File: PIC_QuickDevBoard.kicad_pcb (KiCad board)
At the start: 2 copper layers, 70.9 x 81.3 mm, 36 parts, among them J1 Conn_01x08_Pin, J10 VCC Lines, J2 Conn_01x08_Pin, J3 Conn_01x08_Pin, J4 PowerSource, J5 PICKitConnector, J6 USB_B_Micro, J7 PGEC_LINES, J8 PGED_LINES, J9 MCLR_LINES, SW1 SW_Push, U1 PIC24F, U2 PIC16F84, U3 LDA33A, U4 PIC16F1459-IP, Y1 Crystal

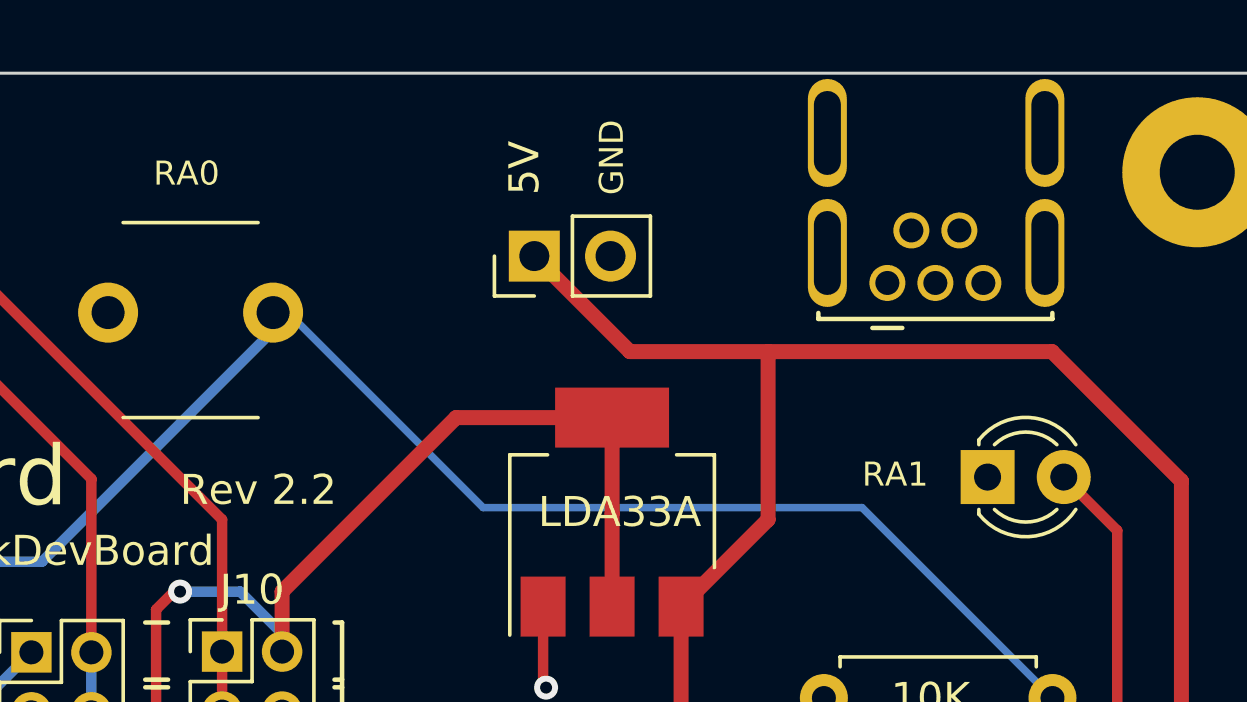
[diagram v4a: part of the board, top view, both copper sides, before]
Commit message: Rev2.3 - fixed mini-usb footprint and pcb routing power from it.
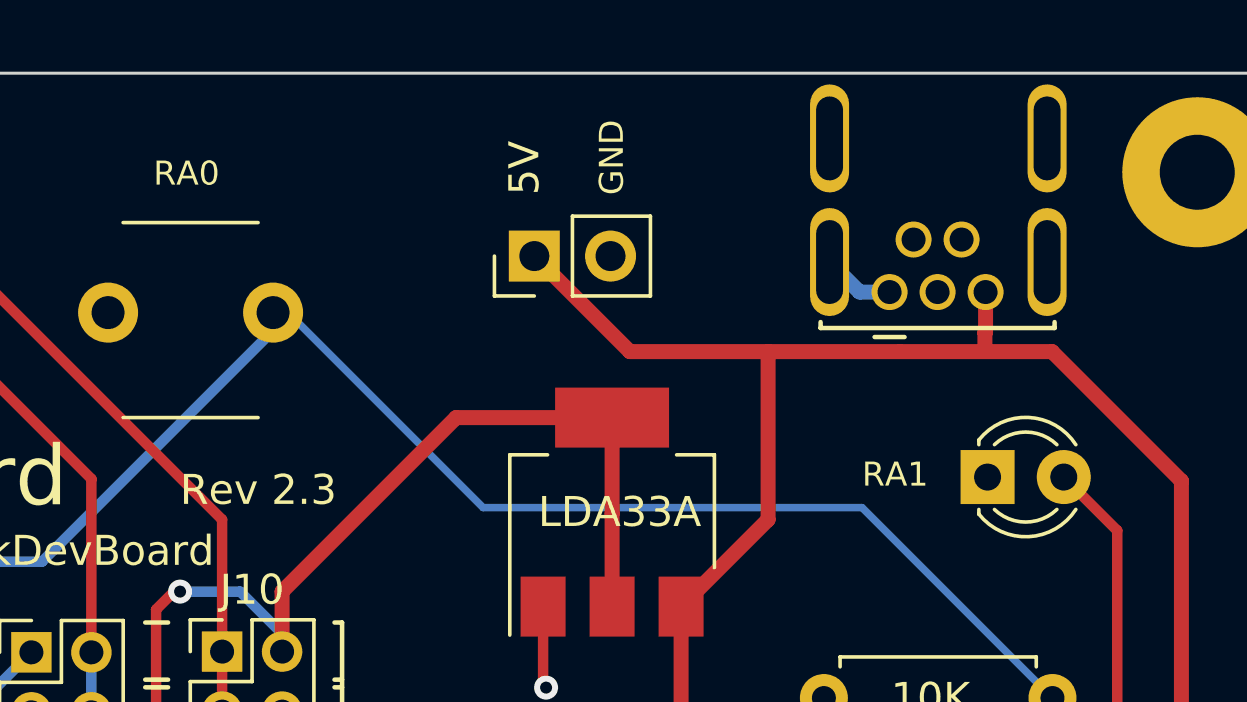
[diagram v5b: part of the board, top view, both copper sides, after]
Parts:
- moved J6 0.31 mm to (120.3, 40.3)
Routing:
- net GND: track 242.6 -> 245.1 mm
- net +5V: track 136.7 -> 138.7 mm
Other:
- board text added: "Rev 2.3"
- board text removed: "Rev 2.2"
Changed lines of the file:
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@@
 	(title_block
 		(title "PIC16/24 Programmer & Dev Board")
-		(date "2024-05-01")
-		(rev "2.2")
+		(date "2024-05-17")
+		(rev "2.3")
 		(company "RCC 2024")
 	)
@@
 	(net 39 "+5V")
 	(net 40 "+3.3V")
+	(net 41 "unconnected-(J6-ID-Pad4)")
+	(net 42 "unconnected-(J6-D--Pad2)")
+	(net 43 "unconnected-(J6-D+-Pad3)")
 	(footprint "Connector_PinHeader_2.00mm:PinHeader_2x03_P2.00mm_Vertical"
 		(layer "F.Cu")
@@
 	(footprint "Roni_Footprints:USB_Mini-B_Tensility_4Holes"
 		(layer "F.Cu")
-		(at 120.226 40.012)
+		(at 120.299813 40.314672)
 		(descr "http://www.tensility.com/pdffiles/54-00023.pdf")
 		(tags "usb mini receptacle vertical")
@@
 			)
 		)
+		(property ki_fp_filters "USB*")
+		(sheetname "Root")
+		(sheetfile "PIC_QuickDevBoard.kicad_sch")
 		(attr through_hole)
 		(fp_line
@@
 		)
 		(fp_line
-			(start -2.8 -6.82681)
+			(start -2.8 -7)
 			(end -2.8 1.5)
 			(stroke
@@
 		)
 		(fp_line
-			(start 6 -6.82681)
-			(end -2.8 -6.82681)
+			(start 6 -7)
+			(end -2.8 -7)
 			(stroke
 				(width 0.05)
@@
 		(fp_line
 			(start 6 1.5)
-			(end 6 -6.82681)
+			(end 6 -7)
 			(stroke
 				(width 0.05)
@@
 			)
 		)
-		(pad "" thru_hole circle
-			(at 0 0)
+		(pad "1" thru_hole circle
+			(at 3.2 0)
 			(size 1.2 1.2)
 			(drill 0.8)
 			(layers "*.Cu" "*.Mask")
 			(remove_unused_layers no)
+			(net 39 "+5V")
+			(pinfunction "VBUS")
+			(pintype "power_out")
 		)
-		(pad "" thru_hole circle
-			(at 0.8 -1.75)
+		(pad "2" thru_hole circle
+			(at 2.4 -1.75)
 			(size 1.2 1.2)
 			(drill 0.8)
 			(layers "*.Cu" "*.Mask")
 			(remove_unused_layers no)
+			(net 42 "unconnected-(J6-D--Pad2)")
+			(pinfunction "D-")
+			(pintype "bidirectional+no_connect")
 		)
-		(pad "" thru_hole circle
+		(pad "3" thru_hole circle
 			(at 1.6 0)
 			(size 1.2 1.2)
@@
 			(layers "*.Cu" "*.Mask")
 			(remove_unused_layers no)
+			(net 43 "unconnected-(J6-D+-Pad3)")
+			(pinfunction "D+")
+			(pintype "bidirectional+no_connect")
 		)
-		(pad "" thru_hole circle
-			(at 2.4 -1.75)
+		(pad "4" thru_hole circle
+			(at 0.8 -1.75)
 			(size 1.2 1.2)
 			(drill 0.8)
 			(layers "*.Cu" "*.Mask")
 			(remove_unused_layers no)
+			(net 41 "unconnected-(J6-ID-Pad4)")
+			(pinfunction "ID")
+			(pintype "passive+no_connect")
 		)
-		(pad "" thru_hole circle
-			(at 3.2 0)
+		(pad "5" thru_hole circle
+			(at 0 0)
 			(size 1.2 1.2)
 			(drill 0.8)
 			(layers "*.Cu" "*.Mask")
 			(remove_unused_layers no)
+			(net 1 "GND")
+			(pinfunction "GND")
+			(pintype "power_out")
 		)
 		(pad "6" thru_hole oval
-			(at -2 -5)
+			(at -2 -5.120687)
 			(size 1.3 3.6)
 			(drill oval 0.9 2.8)
@@
 		)
 		(pad "6" thru_hole oval
-			(at 5.25 -5)
+			(at 5.25 -5.120687)
 			(size 1.3 3.6)
 			(drill oval 0.9 2.8)
@@
 		)
 	)
-	(gr_text "Rev 2.2"
+	(gr_text "Rev 2.3"
 		(at 96.647 47.498 0)
 		(layer "F.SilkS")
@@
 	)
 	(segment
+		(start 120.222677 40.391808)
+		(end 120.299813 40.314672)
+		(width 0.5)
+		(layer "F.Cu")
+		(net 1)
+	)
+	(segment
 		(start 79.883 71.374)
 		(end 80.137 71.12)
@@
 	)
 	(segment
+		(start 119.299813 40.314672)
+		(end 118.299813 39.314672)
+		(width 0.5)
+		(layer "B.Cu")
+		(net 1)
+	)
+	(segment
 		(start 126.85 84.7)
 		(end 126.85 85.956)
@@
 	)
 	(segment
+		(start 120.299813 40.314672)
+		(end 119.299813 40.314672)
+		(width 0.5)
+		(layer "B.Cu")
+		(net 1)
+	)
+	(segment
 		(start 93.091 82.296)
 		(end 93.091 78.319)
@@
 	)
 	(segment
-		(start 125.714 42.3)
-		(end 116.25 42.3)
-		(width 0.5)
-		(layer "F.Cu")
-		(net 39)
-	)
-	(segment
 		(start 110.85 56.9)
 		(end 113.35 54.4)
@@
 	)
 	(segment
+		(start 123.499813 41.645167)
+		(end 123.499813 40.314672)
+		(width 0.5)
+		(layer "F.Cu")
+		(net 39)
+	)
+	(segment
 		(start 108.458 39.116)
 		(end 108.234 39.116)
@@
 	)
 	(segment
+		(start 125.714 42.3)
+		(end 123.476461 42.3)
+		(width 0.5)
+		(layer "F.Cu")
+		(net 39)
+	)
+	(segment
 		(start 115.25 111.3)
 		(end 130.028 96.522)
@@
 	)
 	(segment
+		(start 123.476461 42.3)
+		(end 120.65 42.3)
+		(width 0.5)
+		(layer "F.Cu")
+		(net 39)
+	)
+	(segment
 		(start 107.05 111.3)
 		(end 115.25 111.3)
@@
 	)
 	(segment
+		(start 123.476461 42.3)
+		(end 123.476461 41.668519)
+		(width 0.5)
+		(layer "F.Cu")
+		(net 39)
+	)
+	(segment
 		(start 116.25 42.3)
 		(end 111.642 42.3)
 		(width 0.5)
 		(layer "F.Cu")
+		(net 39)
+	)
+	(segment
+		(start 123.476461 41.668519)
+		(end 123.499813 41.645167)
+		(width 0.5)
+		(layer "F.Cu")
+		(net 39)
+	)
+	(segment
+		(start 120.65 42.3)
+		(end 116.25 42.3)
+		(width 0.5)
+		(layer "F.Cu")

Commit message: Rev2.3 - led on RB4 and Demo for all three suported PICs
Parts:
- R3: value 270 -> 10K
- R4: value 270 -> 470R
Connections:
- R4 pad 1: RA1 -> RB4
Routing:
- net RB4: track 62.5 -> 104.6 mm
- net RA1: track 98.8 -> 75.5 mm
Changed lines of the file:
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@@
 	(title_block
 		(title "PIC16/24 Programmer & Dev Board")
-		(date "2024-05-17")
+		(date "2024-05-19")
 		(rev "2.3")
 		(company "RCC 2024")
@@
 			)
 		)
-		(property "Value" "270"
+		(property "Value" "470R"
 			(at 3.556 0 0)
 			(layer "F.SilkS")
@@
 			(layers "*.Cu" "*.Mask")
 			(remove_unused_layers no)
-			(net 25 "RA1")
+			(net 16 "RB4")
 			(pintype "passive")
 		)
@@
 			)
 		)
-		(property "Value" "270"
+		(property "Value" "10K"
 			(at 4.064 0 -90)
 			(layer "F.SilkS")
@@
 		)
 	)
-	(gr_text "RA1"
+	(gr_text "RB4"
 		(at 119.38 46.863 0)
 		(layer "F.SilkS")
@@
 	)
 	(segment
+		(start 127.537999 66.716629)
+		(end 127.537999 81.910849)
+		(width 0.25)
+		(layer "F.Cu")
+		(net 16)
+	)
+	(segment
 		(start 108.059 93.581)
 		(end 123.807 93.581)
@@
 	)
 	(segment
+		(start 127.537999 81.910849)
+		(end 125.83322 83.615628)
+		(width 0.25)
+		(layer "F.Cu")
+		(net 16)
+	)
+	(segment
 		(start 92.816774 92.855)
 		(end 104.503 92.855)
@@
 	)
 	(segment
+		(start 123.807 84.370009)
+		(end 123.807 93.581)
+		(width 0.25)
+		(layer "F.Cu")
+		(net 16)
+	)
+	(segment
+		(start 124.561381 83.615628)
+		(end 123.807 84.370009)
+		(width 0.25)
+		(layer "F.Cu")
+		(net 16)
+	)
+	(segment
+		(start 125.83322 83.615628)
+		(end 124.561381 83.615628)
+		(width 0.25)
+		(layer "F.Cu")
+		(net 16)
+	)
+	(segment
 		(start 104.503 92.855)
 		(end 105.918 91.44)
@@
 	)
 	(segment
+		(start 119.24137 58.42)
+		(end 127.537999 66.716629)
+		(width 0.25)
+		(layer "F.Cu")
+		(net 16)
+	)
+	(segment
+		(start 118.11 58.42)
+		(end 119.24137 58.42)
+		(width 0.25)
+		(layer "F.Cu")
+		(net 16)
+	)
+	(segment
 		(start 78.885 95.395)
 		(end 90.276774 95.395)
@@
 	)
 	(segment
-		(start 127.466 72.432)
-		(end 125.222 74.676)
-		(width 0.35)
-		(layer "B.Cu")
-		(net 25)
-	)
-	(segment
 		(start 70.979014 62.790069)
 		(end 70.979014 60.819014)
@@
 		(layer "B.Cu")
 		(net 25)
-	)
-	(segment
-		(start 121.92 58.42)
-		(end 127.466 63.966)
-		(width 0.35)
-		(layer "B.Cu")
-		(net 25)
-	)
-	(segment
-		(start 127.466 63.966)
-		(end 127.466 72.432)
-		(width 0.35)
-		(layer "B.Cu")
-		(net 25)
-	)
-	(segment
-		(start 118.11 58.42)
-		(end 121.92 58.42)
-		(width 0.35)
-		(layer "B.Cu")
-		(net 25)
